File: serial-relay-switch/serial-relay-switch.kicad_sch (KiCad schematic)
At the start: 55 parts, among them J1 Screw_Terminal_01x01, J10 Screw_Terminal_01x01, J11 Screw_Terminal_01x01, J12 Conn_01x01, J13 Conn_01x01, J14 Conn_01x01, J15 Screw_Terminal_01x01, J16 Screw_Terminal_01x01, J17 Conn_01x01, J18 Conn_01x01, J2 2501551-4, J3 Conn_01x01, J4 Screw_Terminal_01x01, J5 Screw_Terminal_01x01, J6 Screw_Terminal_01x01, J7 Screw_Terminal_01x01, J8 Screw_Terminal_01x01, J9 Screw_Terminal_01x01, K1 G2RL-1-E, K2 G2RL-1-E, K3 G2RL-1-E, K4 G2RL-1-E, K5 G2RL-1-E, K6 G2RL-1-E, U1 H11L1, U10 SZNUD3124LT1G, U2 ISL8488E, U3 SZNUD3124LT1G, U4 ISL8488E, U5 HEF4094B, U6 SZNUD3124LT1G, U7 SZNUD3124LT1G, U8 SZNUD3124LT1G, U9 SZNUD3124LT1G

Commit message: [rs] Most of schematic complete
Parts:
- removed J12, J13, J14, J3: Conn_01x01, CUSTOM:Pin_D1.0mm, symbol Connector_Generic:Conn_01x01
- removed R23, R26: 10k, Resistor_SMD:R_0603_1608Metric, symbol CUSTOM:R
- removed R29: 120, Resistor_SMD:R_0603_1608Metric, symbol CUSTOM:R
- added J19, J20: Screw_Terminal_01x01, CUSTOM:8195, symbol Connector:Screw_Terminal_01x01
- added J21: Conn_01x01, CUSTOM:Pin_D1.0mm, symbol Connector_Generic:Conn_01x01
- added K7, K8: G2RL-1-E, Relay_THT:Relay_SPDT_Omron_G2RL-1-E, symbol Relay:G2RL-1-E
- added U11, U12: SZNUD3124LT1G, Package_TO_SOT_SMD:SOT-23, symbol CUSTOM:SZNUD3124LT1G
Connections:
- net SCAN_OUT is gone; now on net LOAD: U2.3 (DI)
- net +5V: now also U5.15 (OE), U5.16 (V_{DD}), K7.A1, K8.A1; no longer R27.2
- net CLK: now also U4.3 (DI), U5.3 (CP); no longer U4.2 (RO)
- net CLK_N: now also U4.6 (Z); no longer U4.7 (B)
- net CLK_P: now also U4.5 (Y); no longer U4.8 (A)
- net GND: now also J2.12 (LED2+), U5.8 (V_{SS}), U11.2, U12.2; no longer U4.3 (DI)
- net LD_N: now also U2.5 (Y); no longer R25.1, R28.1
- net LD_P: now also U2.6 (Z); no longer R22.2, R28.2
- net LINE: now also K7.11, K8.11
- net SCAN_IN: now also J17.1 (Pin_1), U2.2 (RO), U5.2 (D)
- net OUT_F: now reaches J11.1 (Pin_1), K6.14
- net OUT_B: now reaches J9.1 (Pin_1), K4.14
- net CTL_B: now reaches U8.1
- net CTL_B: now also U5.5 (QP1)
- net OUT_C: now reaches J7.1 (Pin_1), K2.14
- net CTL_E: now reaches U7.1
- net CTL_E: now also U5.14 (QP4)
- net OUT_A: now reaches J6.1 (Pin_1), K1.14
- net CTL_C: now reaches U6.1
- net CTL_C: now also U5.6 (QP2)
- net OUT_D: now reaches J10.1 (Pin_1), K5.14
- net CTL_A: now reaches U3.1
- net CTL_A: now also U5.4 (QP0)
- net CTL_F: now reaches U10.1
- net CTL_F: now also U5.13 (QP5)
- net OUT_E: now reaches J8.1 (Pin_1), K3.14
- net LOAD: now reaches U5.1 (STR)
- net LOAD: now also R27.2, J21.1 (Pin_1)
- net CTL_H: now reaches U5.11 (QP7)
- net CTL_H: now also U12.1
- net CTL_G: now reaches U5.12 (QP6)
- net CTL_G: now also U11.1
- net CTL_D: now reaches U5.7 (QP3)
- net CTL_D: now also U9.1
- removed net LOADB: J17.1 (Pin_1), J2.12 (LED2+), U2.2 (RO)
- net SO_N renamed SI_N
- net SI_N: now also J2.7 (P4+), R25.1, R28.1; no longer J2.8 (P4-)
- net SO_P renamed SI_P
- net SI_P: now also J2.8 (P4-), R22.2, R28.2; no longer J2.7 (P4+)
- new net: K7.A2, U11.3
- new net: K8.A2, U12.3
- new net OUT_G: J19.1 (Pin_1), K7.14
- new net OUT_H: J20.1 (Pin_1), K8.14
- no-connect marks 8 -> 13
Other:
- note added: "* SI defaults LOW"
- note added: "NOTE: To save a gate, the inversion of LOAD to LOADB is performed by twisting the LD diff pair!"
- note added: "NOTE: To simplify board routing, all diff pairs are reversed from standard Ethernet polarity!"
- note removed: "* LOAD defaults LOW (load enabled) * CLK defaults LOW"
- note removed: "AUX ground"
- note removed: "Power for switches"
- note removed: "To chain boards, no-pop the transceivers and the RJ-45 connector. Use the LOADB, CLK, and SCAN_OUT connections between boards."
- moved on the sheet: C2, C3, C4, C5, C6, H1, H2, H3, H4, J10, J11, J17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

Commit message: [rs] Complete schematic
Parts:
- removed U5: HEF4094B, symbol 4xxx:HEF4094B
- added C10, C7, C8, C9: 0.1uF, Capacitor_SMD:C_0603_1608Metric, symbol CUSTOM:C
- added D2, D3, D4, D5, D6, D7, D8, D9: LED, symbol CUSTOM:LED
- added R1, R2, R3, R4, R5, R6, R7, R8: 1k, symbol CUSTOM:R
- added U13: 74HCT595, Package_SO:SOIC-16_3.9x9.9mm_P1.27mm, symbol 74xx:74HCT595
- added U14: 74LVC1G32, symbol 74xGxx:74LVC1G32
- added U15: 74LVC1G08, symbol 74xGxx:74LVC1G08
- added U16: 74LVC1G04, symbol 74xGxx:74LVC1G04
- added U17: 74LS163, symbol 74xx:74LS163
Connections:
- net +5V: now also C10.1, C7.1, C8.1, C9.1, U13.10 (~{SRCLR}), U13.16 (VCC), U14.5 (VCC), U15.5 (VCC), U16.5 (VCC), U17.1 (~{MR}), U17.16 (VCC), U17.6 (D3)
- net CLK: now also U14.2, U16.2, U17.2 (CP)
- net CTL_A: now also R1.1, U13.15 (QA)
- net CTL_B: now also R5.1, U13.1 (QB)
- net CTL_C: now also R3.1, U13.2 (QC)
- net CTL_D: now also R6.1, U13.3 (QD)
- net CTL_E: now also R4.1, U13.4 (QE)
- net CTL_F: now also R7.1, U13.5 (QF)
- net CTL_G: now also R2.1, U13.6 (QG)
- net CTL_H: now also R8.1, U13.7 (QH)
- net GND: now also C10.2, C7.2, C8.2, C9.2, D2.1 (K), D3.1 (K), D4.1 (K), D5.1 (K), D6.1 (K), D7.1 (K), D8.1 (K), D9.1 (K), U13.13 (~{OE}), U13.8 (GND), U14.3 (GND), U15.3 (GND), U16.3 (GND), U17.10 (CET), U17.3 (D0), U17.4 (D1), U17.5 (D2), U17.7 (CEP), U17.8 (GND)
- net LD_N: now also U2.6 (Z); no longer U2.5 (Y)
- net LD_P: now also U2.5 (Y); no longer U2.6 (Z)
- net LINE: now also K1.12, K2.12, K3.12, K4.12, K5.12, K6.12, K7.12, K8.12
- net LOAD: now also U17.11 (Q3), U17.9 (~{PE}); no longer R27.2
- net SCAN_IN: now also U13.14 (SER)
- new net: D5.2 (A), R4.2
- new net: D3.2 (A), R2.2
- new net: D2.2 (A), R1.2
- new net: D4.2 (A), R3.2
- new net: D9.2 (A), R8.2
- new net: D6.2 (A), R5.2
- new net: D8.2 (A), R7.2
- new net: D7.2 (A), R6.2
- new net CLKB: U15.1, U16.4
- new net COUNT_RCO: R27.2, U14.1, U15.2, U17.15 (TC)
- new net OUTPUT_UPDATE: U13.12 (RCLK), U15.4
- new net RECEIVE_CLK: U13.11 (SRCLK), U14.4
- no-connect marks 13 -> 7
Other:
- note added: "LEDs are BiColor. PWR should be Green. RCO should be Yellow."
- note added: "NOTE: To simplify board routing, all signal diff pairs are reversed from standard Ethernet polarity!"
- note removed: "LEDs are BiColor. PWR should be Green. LOAD should be Yellow."
- note removed: "NOTE: To save a gate, the inversion of LOAD to LOADB is performed by twisting the LD diff pair!"
- note removed: "NOTE: To simplify board routing, all diff pairs are reversed from standard Ethernet polarity!"
- moved on the sheet: C2, H1, H2, H3, H4, J1, J10, J11, J15, J16, J19, J20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

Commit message: [rs] Footprint assignment
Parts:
- D1: footprint (none) -> Diode_SMD:D_SOD-123F
- D2, D3, D4, D5, D6, D7, D8, D9: footprint (none) -> LED_SMD:LED_0603_1608Metric
- R1, R2, R3, R4, R5, R6, R7, R8: footprint (none) -> Resistor_SMD:R_0603_1608Metric
- U14, U15, U16: footprint (none) -> Package_TO_SOT_SMD:SOT-23-5
- U17: footprint (none) -> Package_SO:SOIC-16_3.9x9.9mm_P1.27mm
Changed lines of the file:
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@@
 			)
 		)
-		(property "Footprint" ""
+		(property "Footprint" "Package_SO:SOIC-16_3.9x9.9mm_P1.27mm"
 			(at 63.5 134.62 0)
 			(hide yes)
@@
 			)
 		)
-		(property "Footprint" ""
+		(property "Footprint" "LED_SMD:LED_0603_1608Metric"
 			(at 297.18 154.94 0)
 			(hide yes)
@@
 			)
 		)
-		(property "Footprint" ""
+		(property "Footprint" "LED_SMD:LED_0603_1608Metric"
 			(at 276.86 203.2 0)
 			(hide yes)
@@
 			)
 		)
-		(property "Footprint" ""
+		(property "Footprint" "Diode_SMD:D_SOD-123F"
 			(at 50.8 58.42 0)
 			(hide yes)
@@
 			)
 		)
-		(property "Footprint" ""
+		(property "Footprint" "Package_TO_SOT_SMD:SOT-23-5"
 			(at 154.94 152.4 0)
 			(hide yes)
@@
 			)
 		)
-		(property "Footprint" ""
+		(property "Footprint" "LED_SMD:LED_0603_1608Metric"
 			(at 297.18 58.42 0)
 			(hide yes)
@@
 			)
 		)
-		(property "Footprint" ""
+		(property "Footprint" "Resistor_SMD:R_0603_1608Metric"
 			(at 284.48 60.198 90)
 			(hide yes)
@@
 			)
 		)
-		(property "Footprint" ""
+		(property "Footprint" "LED_SMD:LED_0603_1608Metric"
 			(at 297.18 106.68 0)
 			(hide yes)
@@
 			)
 		)
-		(property "Footprint" ""
+		(property "Footprint" "Resistor_SMD:R_0603_1608Metric"
 			(at 347.98 204.978 90)
 			(hide yes)
@@
 			)
 		)
-		(property "Footprint" ""
+		(property "Footprint" "Resistor_SMD:R_0603_1608Metric"
 			(at 347.98 60.198 90)
 			(hide yes)
@@
 			)
 		)
-		(property "Footprint" ""
+		(property "Footprint" "Resistor_SMD:R_0603_1608Metric"
 			(at 284.48 156.718 90)
 			(hide yes)
@@
 			)
 		)
-		(property "Footprint" ""
+		(property "Footprint" "Package_TO_SOT_SMD:SOT-23-5"
 			(at 109.22 109.22 0)
 			(hide yes)
@@
 			)
 		)
-		(property "Footprint" ""
+		(property "Footprint" "Resistor_SMD:R_0603_1608Metric"
 			(at 347.98 156.718 90)
 			(hide yes)
@@
 			)
 		)
-		(property "Footprint" ""
+		(property "Footprint" "Resistor_SMD:R_0603_1608Metric"
 			(at 284.48 108.458 90)
 			(hide yes)
@@
 			)
 		)
-		(property "Footprint" ""
+		(property "Footprint" "LED_SMD:LED_0603_1608Metric"
 			(at 360.68 154.94 0)
 			(hide yes)
@@
 			)
 		)
-		(property "Footprint" ""
+		(property "Footprint" "Resistor_SMD:R_0603_1608Metric"
 			(at 347.98 108.458 90)
 			(hide yes)
@@
 			)
 		)
-		(property "Footprint" ""
+		(property "Footprint" "LED_SMD:LED_0603_1608Metric"
 			(at 360.68 58.42 0)
 			(hide yes)
@@
 			)
 		)
-		(property "Footprint" ""
+		(property "Footprint" "LED_SMD:LED_0603_1608Metric"
 			(at 360.68 203.2 0)
 			(hide yes)
@@
 			)
 		)
-		(property "Footprint" ""
+		(property "Footprint" "Package_TO_SOT_SMD:SOT-23-5"
 			(at 154.94 111.76 0)
 			(hide yes)
@@
 			)
 		)
-		(property "Footprint" ""
+		(property "Footprint" "LED_SMD:LED_0603_1608Metric"
 			(at 360.68 106.68 0)
 			(hide yes)
@@
 			)
 		)
-		(property "Footprint" ""
+		(property "Footprint" "Resistor_SMD:R_0603_1608Metric"
 			(at 264.16 204.978 90)
 			(hide yes)

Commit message: [rs] Mostly complete preliminary PCB placement
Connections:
- net LINE: now also R30.1; no longer R30.2
- net at D1.1 (K), U1.1: now also R30.2; no longer R30.1
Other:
- moved on the sheet: R30
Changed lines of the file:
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@@
 	)
 	(junction
+		(at 38.1 27.94)
+		(diameter 0)
+		(color 0 0 0 0)
+	)
+	(junction
 		(at 340.36 198.12)
 		(diameter 0)
@@
 	)
 	(junction
-		(at 38.1 27.94)
-		(diameter 0)
-		(color 0 0 0 0)
-	)
-	(junction
 		(at 101.6 228.6)
 		(diameter 0)
@@
 	(wire
 		(pts
-			(xy 38.1 53.34) (xy 38.1 48.26)
-		)
-		(stroke
-			(width 0)
-			(type default)
-		)
-	)
-	(wire
-		(pts
 			(xy 35.56 33.02) (xy 40.64 33.02)
 		)
@@
 	(wire
 		(pts
-			(xy 35.56 27.94) (xy 40.64 27.94)
+			(xy 35.56 27.94) (xy 38.1 27.94)
 		)
 		(stroke
@@
 	(wire
 		(pts
-			(xy 38.1 40.64) (xy 38.1 27.94)
+			(xy 38.1 27.94) (xy 38.1 40.64)
 		)
 		(stroke
@@
 	(wire
 		(pts
+			(xy 38.1 48.26) (xy 38.1 53.34)
+		)
+		(stroke
+			(width 0)
+			(type default)
+		)
+	)
+	(wire
+		(pts
 			(xy 391.16 17.78) (xy 327.66 17.78)
 		)
@@
 	(wire
 		(pts
+			(xy 38.1 27.94) (xy 40.64 27.94)
+		)
+		(stroke
+			(width 0)
+			(type default)
+		)
+	)
+	(wire
+		(pts
 			(xy 317.5 96.52) (xy 327.66 96.52)
 		)
@@
 	(symbol
 		(lib_id "CUSTOM:R")
-		(at 38.1 45.72 180)
+		(at 38.1 43.18 0)
 		(unit 1)
 		(body_style 1)
@@
 		(dnp no)
 		(property "Reference" "R30"
-			(at 36.83 49.53 90)
+			(at 39.37 39.37 90)
 			(show_name no)
 			(do_not_autoplace no)
@@
 		)
 		(property "Value" "100k"
-			(at 36.83 39.37 90)
+			(at 39.37 49.53 90)
 			(show_name no)
 			(do_not_autoplace no)
@@
 		)
 		(property "Footprint" "Resistor_THT:R_Axial_DIN0414_L11.9mm_D4.5mm_P5.08mm_Vertical"
-			(at 39.878 45.72 90)
+			(at 36.322 43.18 90)
 			(hide yes)
 			(show_name no)
@@
 		)
 		(property "Datasheet" ""
-			(at 38.1 45.72 0)
+			(at 38.1 43.18 0)
 			(hide yes)
 			(show_name no)

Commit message: [rs] New preliminary board layout
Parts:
- removed J15, J16: Screw_Terminal_01x01, CUSTOM:8195, symbol Connector:Screw_Terminal_01x01
- added H5: MountingHole, MountingHole:MountingHole_3.2mm_M3, symbol Mechanical:MountingHole
- K1, K2, K3, K4, K5, K6, K7, K8: footprint Relay_THT:Relay_SPDT_Omron_G2RL-1-E -> CUSTOM:Relay_SPDT_Omron_G2RL-1-E
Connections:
- net NEUTRAL: now also D1.1 (K), U1.1; no longer D1.2 (A), U1.2
- new net: D1.2 (A), R30.2, U1.2
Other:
- moved on the sheet: R30

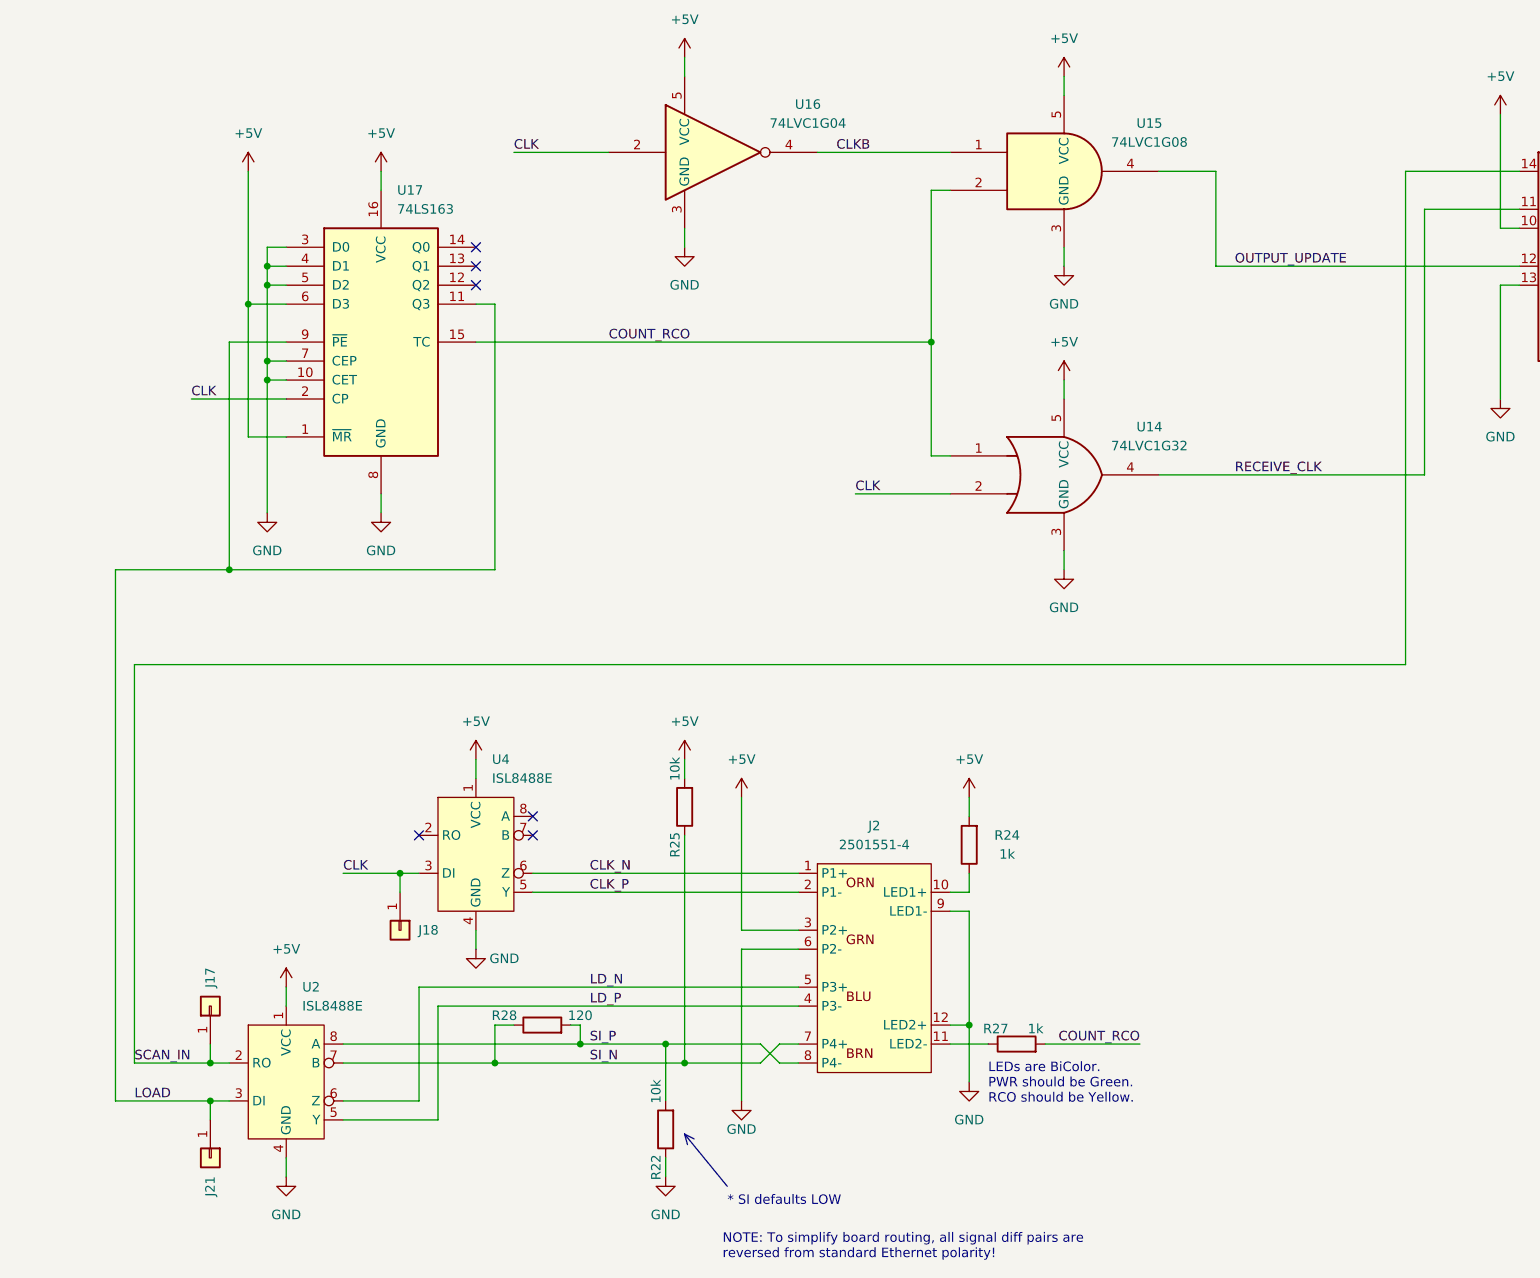
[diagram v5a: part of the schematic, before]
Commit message: [rs] Routed, save for the pesky "Unrouted 1"
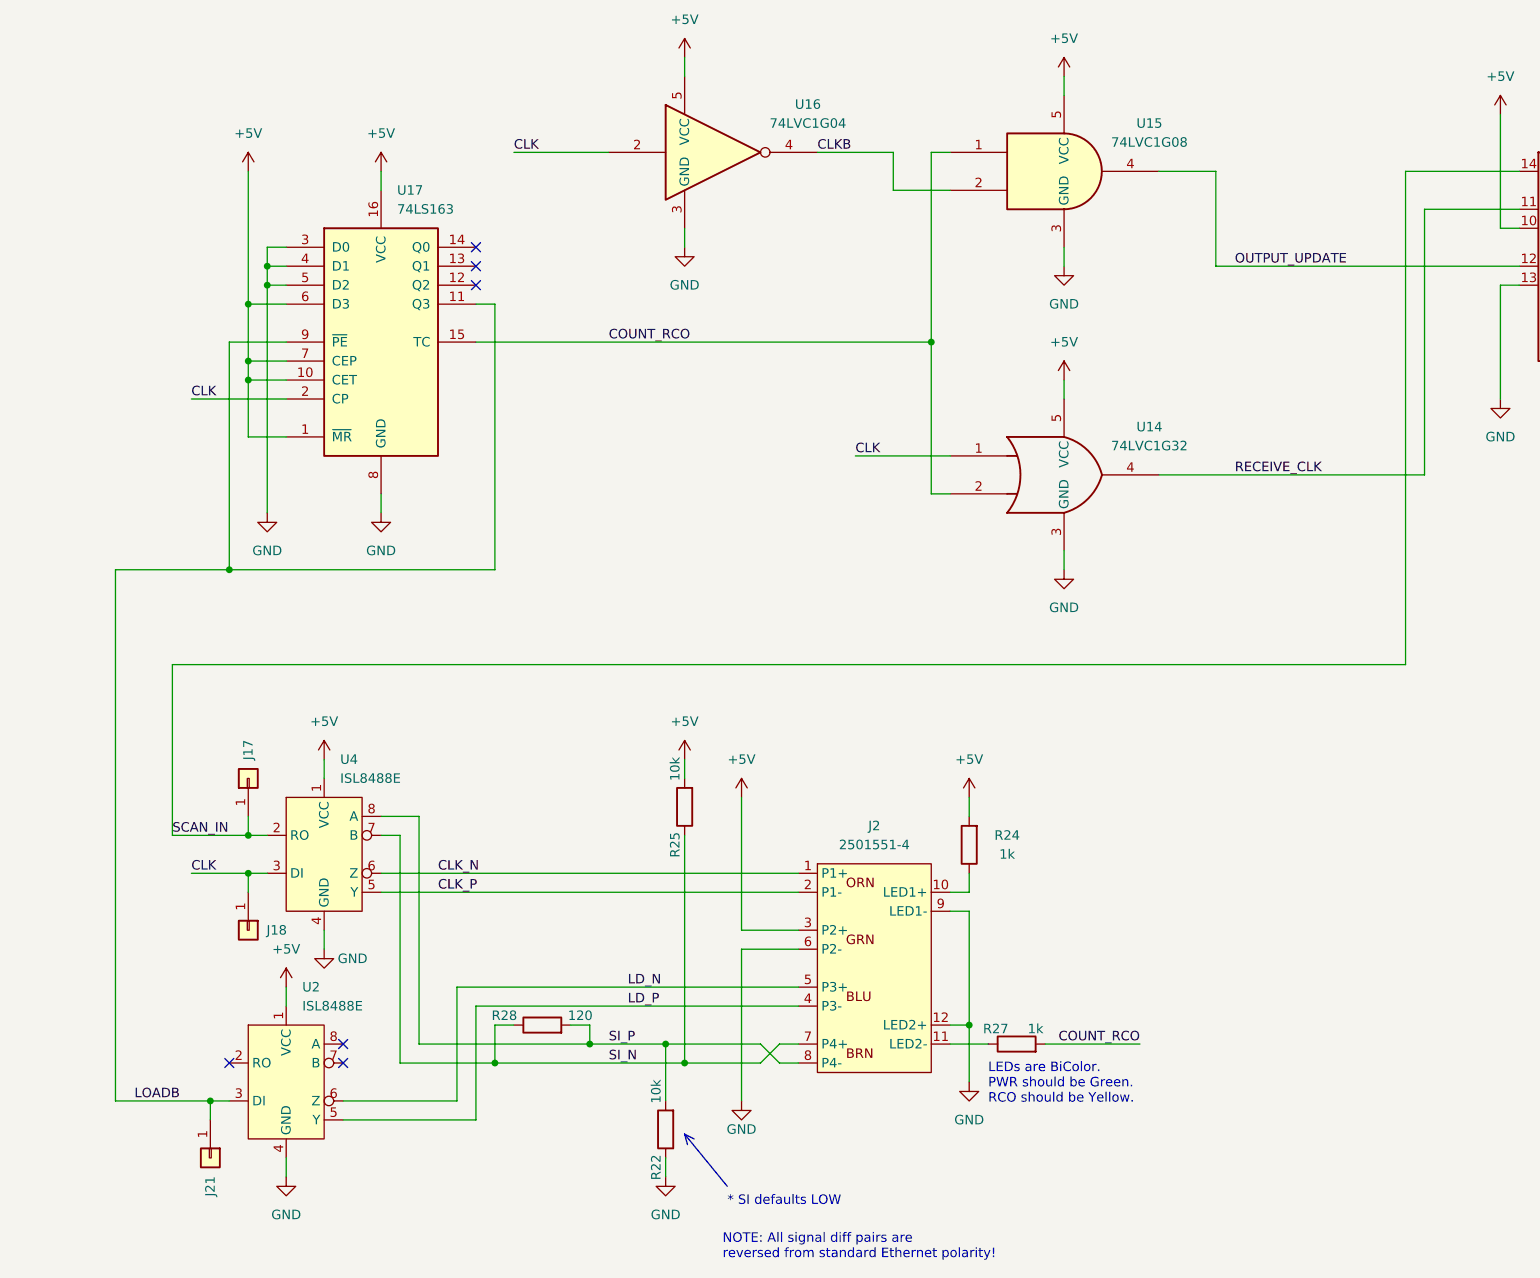
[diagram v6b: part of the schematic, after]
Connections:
- net +5V: now also U17.10 (CET), U17.7 (CEP)
- net CLK: now also U14.1; no longer U14.2
- net CLKB: now also U15.2; no longer U15.1
- net COUNT_RCO: now also U14.2, U15.1; no longer U14.1, U15.2
- net GND: no longer U17.10 (CET), U17.7 (CEP)
- net SCAN_IN: now also U4.2 (RO); no longer U2.2 (RO)
- net SI_N: now also U4.7 (B); no longer U2.7 (B)
- net SI_P: now also U4.8 (A); no longer U2.8 (A)
- net LOAD renamed LOADB
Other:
- note added: "NOTE: All signal diff pairs are reversed from standard Ethernet polarity!"
- note removed: "NOTE: To simplify board routing, all signal diff pairs are reversed from standard Ethernet polarity!"
- moved on the sheet: J17, J18, U4

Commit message: [fp][rs] Change hole footprints to no soldermask
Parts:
- H1, H2, H3, H4, H5: footprint MountingHole:MountingHole_3.2mm_M3 -> CUSTOM:MountingHole_3.2mm_M3
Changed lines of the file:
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@@
 			)
 		)
-		(property "Footprint" "MountingHole:MountingHole_3.2mm_M3"
+		(property "Footprint" "CUSTOM:MountingHole_3.2mm_M3"
 			(at 175.26 35.56 0)
 			(hide yes)
@@
 			)
 		)
-		(property "Footprint" "MountingHole:MountingHole_3.2mm_M3"
+		(property "Footprint" "CUSTOM:MountingHole_3.2mm_M3"
 			(at 175.26 30.48 0)
 			(hide yes)
@@
 			)
 		)
-		(property "Footprint" "MountingHole:MountingHole_3.2mm_M3"
+		(property "Footprint" "CUSTOM:MountingHole_3.2mm_M3"
 			(at 175.26 40.64 0)
 			(hide yes)
@@
 			)
 		)
-		(property "Footprint" "MountingHole:MountingHole_3.2mm_M3"
+		(property "Footprint" "CUSTOM:MountingHole_3.2mm_M3"
 			(at 175.26 25.4 0)
 			(hide yes)
@@
 			)
 		)
-		(property "Footprint" "MountingHole:MountingHole_3.2mm_M3"
+		(property "Footprint" "CUSTOM:MountingHole_3.2mm_M3"
 			(at 175.26 45.72 0)
 			(hide yes)

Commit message: [rs] Check/Finalize PCB; Export gerbers v1.0A0
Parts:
- H3, H5: footprint CUSTOM:MountingHole_3.2mm_M3 -> MountingHole:MountingHole_3.2mm_M3_ISO14580_Pad_TopBottom; symbol Mechanical:MountingHole -> Mechanical:MountingHole_Pad; now left out of the parts list
- H4: footprint CUSTOM:MountingHole_3.2mm_M3 -> MountingHole:MountingHole_3.2mm_M3_DIN965_Pad_TopBottom; symbol Mechanical:MountingHole -> Mechanical:MountingHole_Pad; now left out of the parts list
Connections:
- net GND: now also H3.1, H4.1, H5.1
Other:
- note added: "'166 internal count"
- note added: "'595 internal reg"
- note added: "'595 output reg"
- note added: "CLK"
- note added: "COUNT_RCO"
- note added: "OUTPUT_UPDATE"
- note added: "RECEIVE_CLK"
- note added: "SCAN_IN"
- moved on the sheet: H1, H2
